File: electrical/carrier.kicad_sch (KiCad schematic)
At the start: 30 parts

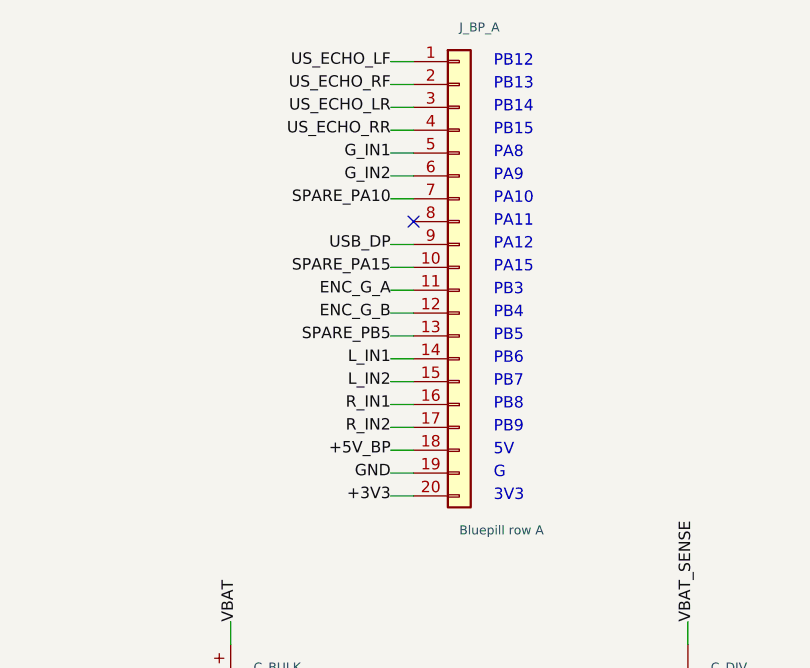
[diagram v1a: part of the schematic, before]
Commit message: fix(electrical): Bluepill row A runs opposite to row B (PB12 faces GND at the USB end)
Co-Authored-By: Claude Opus 5.5 <noreply@anthropic.com>
Claude-Session: https://claude.ai/code/session_01ENsByEFNd15FuMFFPy7PpL
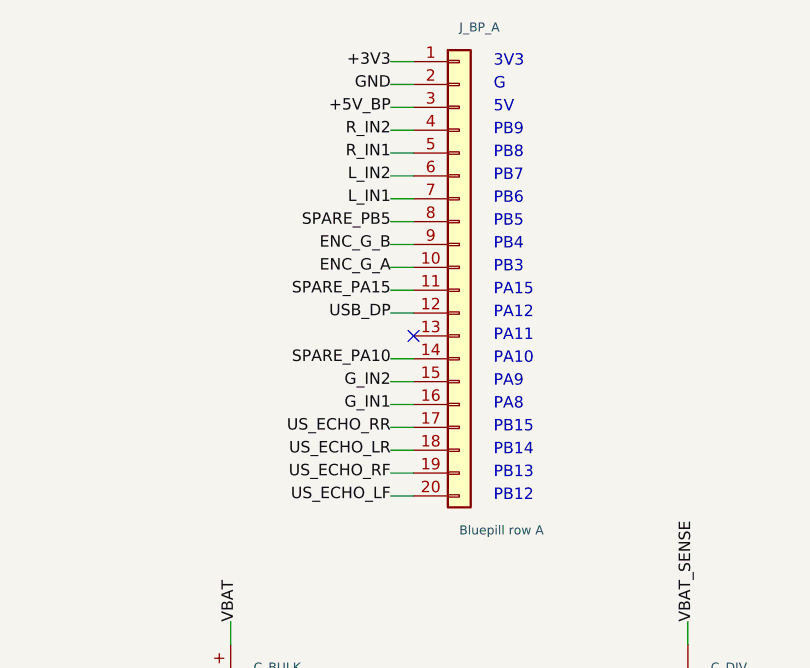
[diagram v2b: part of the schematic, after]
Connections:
- net +3V3: now also J_BP_A.1 (Pin_1); no longer J_BP_A.20 (Pin_20)
- net +5V_BP: now also J_BP_A.3 (Pin_3); no longer J_BP_A.18 (Pin_18)
- net ENC_G_A: now also J_BP_A.10 (Pin_10); no longer J_BP_A.11 (Pin_11)
- net ENC_G_B: now also J_BP_A.9 (Pin_9); no longer J_BP_A.12 (Pin_12)
- net GND: now also J_BP_A.2 (Pin_2); no longer J_BP_A.19 (Pin_19)
- net G_IN1: now also J_BP_A.16 (Pin_16); no longer J_BP_A.5 (Pin_5)
- net G_IN2: now also J_BP_A.15 (Pin_15); no longer J_BP_A.6 (Pin_6)
- net L_IN1: now also J_BP_A.7 (Pin_7); no longer J_BP_A.14 (Pin_14)
- net L_IN2: now also J_BP_A.6 (Pin_6); no longer J_BP_A.15 (Pin_15)
- net R_IN1: now also J_BP_A.5 (Pin_5); no longer J_BP_A.16 (Pin_16)
- net R_IN2: now also J_BP_A.4 (Pin_4); no longer J_BP_A.17 (Pin_17)
- net SPARE_PA10: now also J_BP_A.14 (Pin_14); no longer J_BP_A.7 (Pin_7)
- net SPARE_PA15: now also J_BP_A.11 (Pin_11); no longer J_BP_A.10 (Pin_10)
- net SPARE_PB5: now also J_BP_A.8 (Pin_8); no longer J_BP_A.13 (Pin_13)
- net USB_DP: now also J_BP_A.12 (Pin_12); no longer J_BP_A.9 (Pin_9)
- net US_ECHO_LF: now also J_BP_A.20 (Pin_20); no longer J_BP_A.1 (Pin_1)
- net US_ECHO_LR: now also J_BP_A.18 (Pin_18); no longer J_BP_A.3 (Pin_3)
- net US_ECHO_RF: now also J_BP_A.19 (Pin_19); no longer J_BP_A.2 (Pin_2)
- net US_ECHO_RR: now also J_BP_A.17 (Pin_17); no longer J_BP_A.4 (Pin_4)
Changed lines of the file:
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@@
 (kicad_sch (version 20231120) (generator carrier_gen)
   (paper "A3")
-  (no_connect (at 58.42 45.72))
+  (no_connect (at 58.42 58.42))
   (no_connect (at 160.02 27.94))
   (no_connect (at 160.02 68.58))
@@
     (stroke (width 0.0))
   )
-  (wire (pts (xy 58.42 58.42) (xy 55.88 58.42))
-    (stroke (width 0.0))
-  )
   (wire (pts (xy 58.42 60.96) (xy 55.88 60.96))
     (stroke (width 0.0))
@@
     (stroke (width 0.0))
   )
+  (wire (pts (xy 58.42 45.72) (xy 55.88 45.72))
+    (stroke (width 0.0))
+  )
   (wire (pts (xy 58.42 48.26) (xy 55.88 48.26))
     (stroke (width 0.0))
@@
     (stroke (width 0.0))
   )
-  (text "PB12" (at 67.31 27.94 0)
-    (effects (font (size 1.27 1.27)) (justify left))
-  )
-  (text "PA15" (at 67.31 50.8 0)
-    (effects (font (size 1.27 1.27)) (justify left))
-  )
-  (text "PB3" (at 67.31 53.34 0)
-    (effects (font (size 1.27 1.27)) (justify left))
-  )
-  (text "PB4" (at 67.31 55.88 0)
-    (effects (font (size 1.27 1.27)) (justify left))
-  )
-  (text "PB5" (at 67.31 58.42 0)
-    (effects (font (size 1.27 1.27)) (justify left))
-  )
-  (text "PB6" (at 67.31 60.96 0)
-    (effects (font (size 1.27 1.27)) (justify left))
-  )
-  (text "PB7" (at 67.31 63.5 0)
-    (effects (font (size 1.27 1.27)) (justify left))
-  )
-  (text "PB8" (at 67.31 66.04 0)
-    (effects (font (size 1.27 1.27)) (justify left))
-  )
-  (text "PB9" (at 67.31 68.58 0)
-    (effects (font (size 1.27 1.27)) (justify left))
-  )
-  (text "5V" (at 67.31 71.12 0)
-    (effects (font (size 1.27 1.27)) (justify left))
-  )
-  (text "G" (at 67.31 73.66 0)
-    (effects (font (size 1.27 1.27)) (justify left))
-  )
-  (text "PB13" (at 67.31 30.48 0)
-    (effects (font (size 1.27 1.27)) (justify left))
-  )
-  (text "3V3" (at 67.31 76.2 0)
-    (effects (font (size 1.27 1.27)) (justify left))
-  )
-  (text "PB14" (at 67.31 33.02 0)
-    (effects (font (size 1.27 1.27)) (justify left))
-  )
-  (text "PB15" (at 67.31 35.56 0)
-    (effects (font (size 1.27 1.27)) (justify left))
-  )
-  (text "PA8" (at 67.31 38.1 0)
-    (effects (font (size 1.27 1.27)) (justify left))
-  )
-  (text "PA9" (at 67.31 40.64 0)
-    (effects (font (size 1.27 1.27)) (justify left))
-  )
-  (text "PA10" (at 67.31 43.18 0)
-    (effects (font (size 1.27 1.27)) (justify left))
-  )
-  (text "PA11" (at 67.31 45.72 0)
-    (effects (font (size 1.27 1.27)) (justify left))
-  )
-  (text "PA12" (at 67.31 48.26 0)
+  (text "3V3" (at 67.31 27.94 0)
+    (effects (font (size 1.27 1.27)) (justify left))
+  )
+  (text "PB3" (at 67.31 50.8 0)
+    (effects (font (size 1.27 1.27)) (justify left))
+  )
+  (text "PA15" (at 67.31 53.34 0)
+    (effects (font (size 1.27 1.27)) (justify left))
+  )
+  (text "PA12" (at 67.31 55.88 0)
+    (effects (font (size 1.27 1.27)) (justify left))
+  )
+  (text "PA11" (at 67.31 58.42 0)
+    (effects (font (size 1.27 1.27)) (justify left))
+  )
+  (text "PA10" (at 67.31 60.96 0)
+    (effects (font (size 1.27 1.27)) (justify left))
+  )
+  (text "PA9" (at 67.31 63.5 0)
+    (effects (font (size 1.27 1.27)) (justify left))
+  )
+  (text "PA8" (at 67.31 66.04 0)
+    (effects (font (size 1.27 1.27)) (justify left))
+  )
+  (text "PB15" (at 67.31 68.58 0)
+    (effects (font (size 1.27 1.27)) (justify left))
+  )
+  (text "PB14" (at 67.31 71.12 0)
+    (effects (font (size 1.27 1.27)) (justify left))
+  )
+  (text "PB13" (at 67.31 73.66 0)
+    (effects (font (size 1.27 1.27)) (justify left))
+  )
+  (text "G" (at 67.31 30.48 0)
+    (effects (font (size 1.27 1.27)) (justify left))
+  )
+  (text "PB12" (at 67.31 76.2 0)
+    (effects (font (size 1.27 1.27)) (justify left))
+  )
+  (text "5V" (at 67.31 33.02 0)
+    (effects (font (size 1.27 1.27)) (justify left))
+  )
+  (text "PB9" (at 67.31 35.56 0)
+    (effects (font (size 1.27 1.27)) (justify left))
+  )
+  (text "PB8" (at 67.31 38.1 0)
+    (effects (font (size 1.27 1.27)) (justify left))
+  )
+  (text "PB7" (at 67.31 40.64 0)
+    (effects (font (size 1.27 1.27)) (justify left))
+  )
+  (text "PB6" (at 67.31 43.18 0)
+    (effects (font (size 1.27 1.27)) (justify left))
+  )
+  (text "PB5" (at 67.31 45.72 0)
+    (effects (font (size 1.27 1.27)) (justify left))
+  )
+  (text "PB4" (at 67.31 48.26 0)
     (effects (font (size 1.27 1.27)) (justify left))
   )
@@
     (effects (font (size 1.27 1.27)) (justify left))
   )
-  (label "US_ECHO_LF" (at 55.88 27.94 180)
-    (effects (font (size 1.27 1.27)) (justify right))
-  )
-  (label "SPARE_PA15" (at 55.88 50.8 180)
-    (effects (font (size 1.27 1.27)) (justify right))
-  )
-  (label "ENC_G_A" (at 55.88 53.34 180)
-    (effects (font (size 1.27 1.27)) (justify right))
-  )
-  (label "ENC_G_B" (at 55.88 55.88 180)
-    (effects (font (size 1.27 1.27)) (justify right))
-  )
-  (label "SPARE_PB5" (at 55.88 58.42 180)
-    (effects (font (size 1.27 1.27)) (justify right))
-  )
-  (label "L_IN1" (at 55.88 60.96 180)
-    (effects (font (size 1.27 1.27)) (justify right))
-  )
-  (label "L_IN2" (at 55.88 63.5 180)
-    (effects (font (size 1.27 1.27)) (justify right))
-  )
-  (label "R_IN1" (at 55.88 66.04 180)
-    (effects (font (size 1.27 1.27)) (justify right))
-  )
-  (label "R_IN2" (at 55.88 68.58 180)
-    (effects (font (size 1.27 1.27)) (justify right))
-  )
-  (label "+5V_BP" (at 55.88 71.12 180)
-    (effects (font (size 1.27 1.27)) (justify right))
-  )
-  (label "GND" (at 55.88 73.66 180)
-    (effects (font (size 1.27 1.27)) (justify right))
-  )
-  (label "US_ECHO_RF" (at 55.88 30.48 180)
-    (effects (font (size 1.27 1.27)) (justify right))
-  )
-  (label "+3V3" (at 55.88 76.2 180)
-    (effects (font (size 1.27 1.27)) (justify right))
-  )
-  (label "US_ECHO_LR" (at 55.88 33.02 180)
-    (effects (font (size 1.27 1.27)) (justify right))
-  )
-  (label "US_ECHO_RR" (at 55.88 35.56 180)
-    (effects (font (size 1.27 1.27)) (justify right))
-  )
-  (label "G_IN1" (at 55.88 38.1 180)
-    (effects (font (size 1.27 1.27)) (justify right))
-  )
-  (label "G_IN2" (at 55.88 40.64 180)
-    (effects (font (size 1.27 1.27)) (justify right))
-  )
-  (label "SPARE_PA10" (at 55.88 43.18 180)
-    (effects (font (size 1.27 1.27)) (justify right))
-  )
-  (label "USB_DP" (at 55.88 48.26 180)
-    (effects (font (size 1.27 1.27)) (justify right))
-  )
+  (label "+3V3" (at 55.88 27.94 180)
+    (effects (font (size 1.27 1.27)) (justify right))
+  )
+  (label "ENC_G_A" (at 55.88 50.8 180)
+    (effects (font (size 1.27 1.27)) (justify right))
+  )
+  (label "SPARE_PA15" (at 55.88 53.34 180)
+    (effects (font (size 1.27 1.27)) (justify right))
+  )
+  (label "USB_DP" (at 55.88 55.88 180)
+    (effects (font (size 1.27 1.27)) (justify right))
+  )
+  (label "SPARE_PA10" (at 55.88 60.96 180)
+    (effects (font (size 1.27 1.27)) (justify right))
+  )
+  (label "G_IN2" (at 55.88 63.5 180)
+    (effects (font (size 1.27 1.27)) (justify right))
+  )
+  (label "G_IN1" (at 55.88 66.04 180)
+    (effects (font (size 1.27 1.27)) (justify right))
+  )
+  (label "US_ECHO_RR" (at 55.88 68.58 180)
+    (effects (font (size 1.27 1.27)) (justify right))
+  )
+  (label "US_ECHO_LR" (at 55.88 71.12 180)
+    (effects (font (size 1.27 1.27)) (justify right))
+  )
+  (label "US_ECHO_RF" (at 55.88 73.66 180)
+    (effects (font (size 1.27 1.27)) (justify right))
+  )
+  (label "GND" (at 55.88 30.48 180)
+    (effects (font (size 1.27 1.27)) (justify right))
+  )
+  (label "US_ECHO_LF" (at 55.88 76.2 180)
+    (effects (font (size 1.27 1.27)) (justify right))
+  )
+  (label "+5V_BP" (at 55.88 33.02 180)
+    (effects (font (size 1.27 1.27)) (justify right))
+  )
+  (label "R_IN2" (at 55.88 35.56 180)
+    (effects (font (size 1.27 1.27)) (justify right))
+  )
+  (label "R_IN1" (at 55.88 38.1 180)
+    (effects (font (size 1.27 1.27)) (justify right))
+  )
+  (label "L_IN2" (at 55.88 40.64 180)
+    (effects (font (size 1.27 1.27)) (justify right))
+  )
+  (label "L_IN1" (at 55.88 43.18 180)
+    (effects (font (size 1.27 1.27)) (justify right))
+  )
+  (label "SPARE_PB5" (at 55.88 45.72 180)
+    (effects (font (size 1.27 1.27)) (justify right))
+  )
+  (label "ENC_G_B" (at 55.88 48.26 180)
+    (effects (font (size 1.27 1.27)) (justify right))
+  )

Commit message: electrical: bus layout with a perimeter GND ring
Every cable connector now has pin 1 = GND and stands at right angles to
the board edge with pin 1 on the perimeter, where a bare GND ring on the
solder side picks them all up. J_BUCK shrinks to 3 pins. Insulated wires
drop from 45 to 34 and bare traces from 63 to 45 (ring included).
perfboard.md gains a cable pin-order table for crimping.

Co-Authored-By: Claude Opus 5.5 <noreply@anthropic.com>
Claude-Session: https://claude.ai/code/session_01ENsByEFNd15FuMFFPy7PpL
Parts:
- J_BUCK: footprint Connector_JST:JST_XH_B4B-XH-A_1x04_P2.50mm_Vertical -> Connector_JST:JST_XH_B3B-XH-A_1x03_P2.50mm_Vertical; symbol Connector_Generic:Conn_01x04 -> Connector_Generic:Conn_01x03
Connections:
- net +3V3: now also J_ENC_G.2 (Pin_2), J_ENC_L.2 (Pin_2), J_ENC_R.2 (Pin_2), J_I2C.2 (Pin_2), J_UART.2 (Pin_2); no longer J_ENC_G.1 (Pin_1), J_ENC_L.1 (Pin_1), J_ENC_R.1 (Pin_1), J_I2C.1 (Pin_1), J_UART.1 (Pin_1)
- net +5V: now also J_US_LF.2 (Pin_2), J_US_LR.2 (Pin_2), J_US_RF.2 (Pin_2), J_US_RR.2 (Pin_2); no longer J_US_LF.1 (Pin_1), J_US_LR.1 (Pin_1), J_US_RF.1 (Pin_1), J_US_RR.1 (Pin_1)
- net GND: now also J_BUCK.1 (Pin_1), J_DRV_G.1 (Pin_1), J_DRV_L.1 (Pin_1), J_DRV_R.1 (Pin_1), J_ENC_G.1 (Pin_1), J_ENC_L.1 (Pin_1), J_ENC_R.1 (Pin_1), J_I2C.1 (Pin_1), J_PWR.1 (Pin_1), J_UART.1 (Pin_1), J_US_LF.1 (Pin_1), J_US_LR.1 (Pin_1), J_US_RF.1 (Pin_1), J_US_RR.1 (Pin_1), J_VM_G.1 (Pin_1), J_VM_L.1 (Pin_1), J_VM_R.1 (Pin_1); no longer J_BUCK.2 (Pin_2), J_BUCK.4 (Pin_4), J_DRV_G.3 (Pin_3), J_DRV_L.3 (Pin_3), J_DRV_R.3 (Pin_3), J_ENC_G.2 (Pin_2), J_ENC_L.2 (Pin_2), J_ENC_R.2 (Pin_2), J_I2C.4 (Pin_4), J_PWR.2 (Pin_2), J_UART.4 (Pin_4), J_US_LF.4 (Pin_4), J_US_LR.4 (Pin_4), J_US_RF.4 (Pin_4), J_US_RR.4 (Pin_4), J_VM_G.2 (Pin_2), J_VM_L.2 (Pin_2), J_VM_R.2 (Pin_2)
- net G_IN1: now also J_DRV_G.2 (Pin_2); no longer J_DRV_G.1 (Pin_1)
- net G_IN2: now also J_DRV_G.3 (Pin_3); no longer J_DRV_G.2 (Pin_2)
- net I2C_SCL: now also J_I2C.3 (Pin_3); no longer J_I2C.2 (Pin_2)
- net I2C_SDA: now also J_I2C.4 (Pin_4); no longer J_I2C.3 (Pin_3)
- net L_IN1: now also J_DRV_L.2 (Pin_2); no longer J_DRV_L.1 (Pin_1)
- net L_IN2: now also J_DRV_L.3 (Pin_3); no longer J_DRV_L.2 (Pin_2)
- net R_IN1: now also J_DRV_R.2 (Pin_2); no longer J_DRV_R.1 (Pin_1)
- net R_IN2: now also J_DRV_R.3 (Pin_3); no longer J_DRV_R.2 (Pin_2)
- net UART_RX: now also J_UART.4 (Pin_4); no longer J_UART.3 (Pin_3)
- net UART_TX: now also J_UART.3 (Pin_3); no longer J_UART.2 (Pin_2)
- net US_ECHO_LF_RAW: now also J_US_LF.4 (Pin_4); no longer J_US_LF.3 (Pin_3)
- net US_ECHO_LR_RAW: now also J_US_LR.4 (Pin_4); no longer J_US_LR.3 (Pin_3)
- net US_ECHO_RF_RAW: now also J_US_RF.4 (Pin_4); no longer J_US_RF.3 (Pin_3)
- net US_ECHO_RR_RAW: now also J_US_RR.4 (Pin_4); no longer J_US_RR.3 (Pin_3)
- net US_TRIG_F: now also J_US_LF.3 (Pin_3), J_US_RF.3 (Pin_3); no longer J_US_LF.2 (Pin_2), J_US_RF.2 (Pin_2)
- net US_TRIG_R: now also J_US_LR.3 (Pin_3), J_US_RR.3 (Pin_3); no longer J_US_LR.2 (Pin_2), J_US_RR.2 (Pin_2)
- net VBAT: now also J_BUCK.2 (Pin_2), J_PWR.2 (Pin_2), J_VM_G.2 (Pin_2), J_VM_L.2 (Pin_2), J_VM_R.2 (Pin_2); no longer J_BUCK.1 (Pin_1), J_PWR.1 (Pin_1), J_VM_G.1 (Pin_1), J_VM_L.1 (Pin_1), J_VM_R.1 (Pin_1)
